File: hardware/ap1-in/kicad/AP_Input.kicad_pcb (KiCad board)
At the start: 2 copper layers, 72 x 56 mm, 66 parts, among them J1 QWIIC ENTRADA, J2 QWIIC SALIDA, J3 I2C, J4 I1-I3, J5 I4-I6, J6 I7-I8, J7 COM, U1 TCA9554PWR

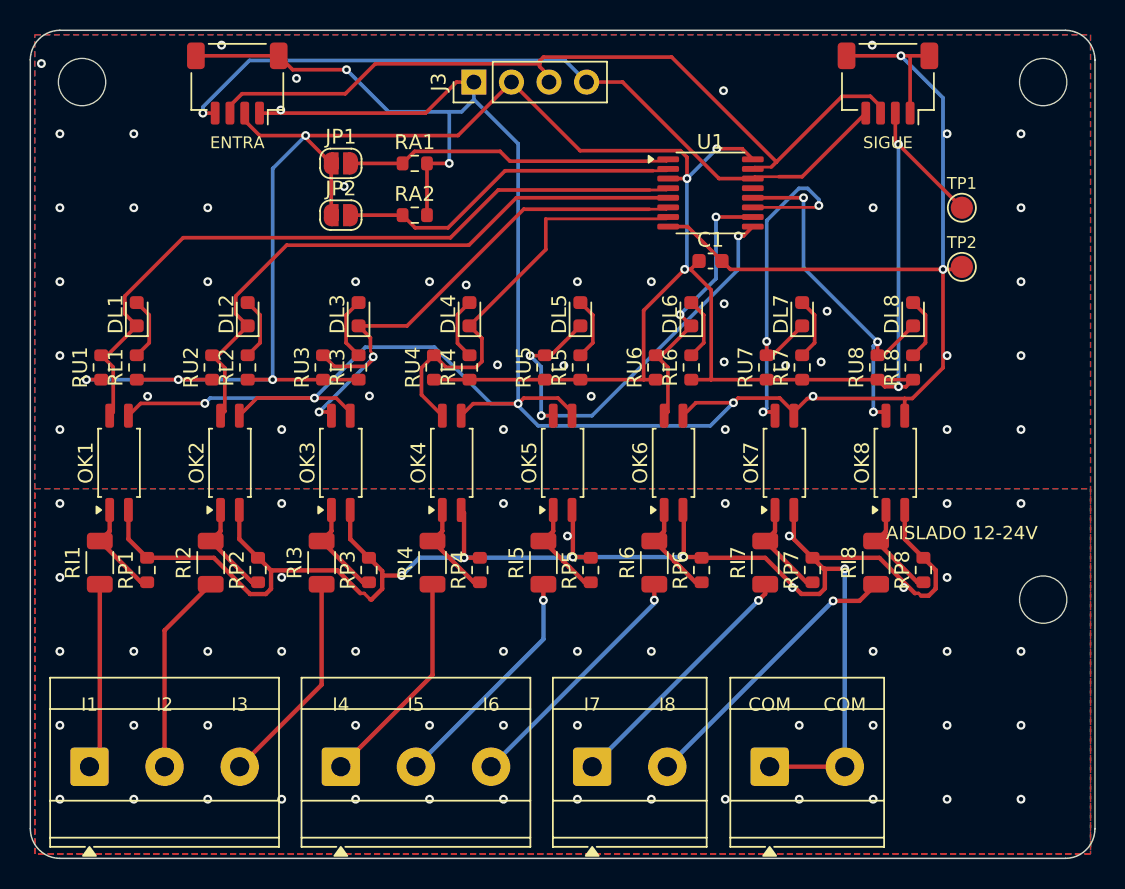
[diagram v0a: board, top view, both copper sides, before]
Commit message: AP CONNECT: sin borneras en todas las placas, placa nueva AP PRO AI4 y guía de fabricantes
- Borneras de tornillo reemplazadas por conectores con cable y código LCSC verificado:
  XT60 (C98732), JST VH 2/3/4 (C160315/6/7), JST XH 2/3/4 (C158012, C144394/5), Qwiic
  en BASE, IND, PIX, DMX, PLANTILLA, AP INPUT, AP OUTPUT y DIST 4; zonas de potencia rehechas
- XT60 de la DIST 4 con la polaridad marcada en la huella (pata 1 = -, pata 2 = +)
- TCA9554PWR ya con código (C477924)
- ap1-ai4: 4 entradas 0-10 V / 4-20 mA con ADS1115 (C37593), +24 V para sensores de lazo
- Programa 1.7: lectura AI4, umbrales con acciones, Home Assistant, tarjeta en la app
- FABRICANTES.md: JLCPCB, PCBWay, Seeed, NextPCB, México; impresión 3D y tornillería
- Pedido JLCPCB con 10 placas (AP-0.2 retirada); ERC/DRC/DFM 0 en todas

Co-Authored-By: Claude Opus 5.5 <noreply@anthropic.com>
Claude-Session: https://claude.ai/code/session_01WVk3oGwfQfGTmAT2PMp8oW
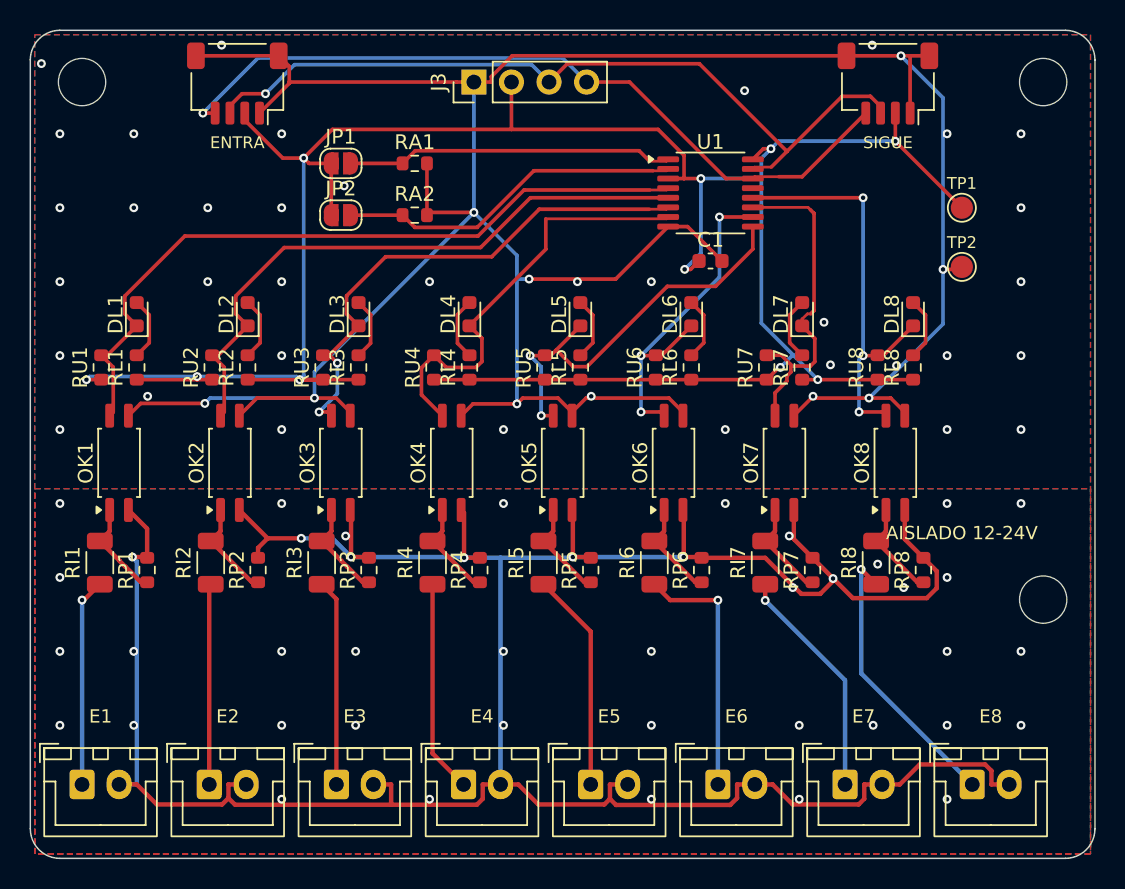
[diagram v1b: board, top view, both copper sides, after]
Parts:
- added J10: E7, Connector_JST:JST_XH_B2B-XH-A_1x02_P2.50mm_Vertical, F.Cu at (155.1, 151.0)
- added J11: E8, Connector_JST:JST_XH_B2B-XH-A_1x02_P2.50mm_Vertical, F.Cu at (163.7, 151.0)
- added J8: E5, Connector_JST:JST_XH_B2B-XH-A_1x02_P2.50mm_Vertical, F.Cu at (137.9, 151.0)
- added J9: E6, Connector_JST:JST_XH_B2B-XH-A_1x02_P2.50mm_Vertical, F.Cu at (146.5, 151.0)
- J4: value I1-I3 -> E1; footprint TerminalBlock_Phoenix:TerminalBlock_Phoenix_MKDS-3-3-5.08_1x03_P5.08mm_Horizontal -> Connector_JST:JST_XH_B2B-XH-A_1x02_P2.50mm_Vertical
- J5: value I4-I6 -> E2; footprint TerminalBlock_Phoenix:TerminalBlock_Phoenix_MKDS-3-3-5.08_1x03_P5.08mm_Horizontal -> Connector_JST:JST_XH_B2B-XH-A_1x02_P2.50mm_Vertical
- J6: value I7-I8 -> E3; footprint TerminalBlock_Phoenix:TerminalBlock_Phoenix_MKDS-3-2-5.08_1x02_P5.08mm_Horizontal -> Connector_JST:JST_XH_B2B-XH-A_1x02_P2.50mm_Vertical
- J7: value COM -> E4; footprint TerminalBlock_Phoenix:TerminalBlock_Phoenix_MKDS-3-2-5.08_1x02_P5.08mm_Horizontal -> Connector_JST:JST_XH_B2B-XH-A_1x02_P2.50mm_Vertical
- moved J7 20.7 mm to (129.3, 151.0)
- moved J6 17.3 mm to (120.7, 151.0)
- moved J5 8.98 mm to (112.1, 151.0)
- moved J4 1.30 mm to (103.5, 151.0)
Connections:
- J4 pad 2: /I2 -> /COM
- J5 pad 1: /I4 -> /I2
- J5 pad 2: /I5 -> /COM
- J6 pad 1: /I7 -> /I3
- J6 pad 2: /I8 -> /COM
- J7 pad 1: /COM -> /I4
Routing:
- net /COM: track 119.9 -> 192.2 mm, vias 54 -> 43
- net /GND: track 204.6 -> 197.0 mm, vias 52 -> 46
- net /IN7: track 27.8 -> 22.7 mm, vias 3 -> 0
- net /IN6: track 18.9 -> 23.5 mm, vias 2 -> 3
- net /3V3: track 174.0 -> 170.6 mm, vias 9 -> 10
- net /IN8: track 25.2 -> 28.2 mm
- net /IN5: track 30.4 -> 28.0 mm, vias 3 -> 2
- net /IN3: track 37.0 -> 35.3 mm
- net /I1: track 12.6 -> 14.1 mm, vias 0 -> 1
- net /I7: track 17.2 -> 15.8 mm
- net /I5: track 15.9 -> 14.9 mm, vias 1 -> 0
- net /I3: track 14.6 -> 14.0 mm
- net /SDA: track 54.8 -> 54.2 mm, vias 0 -> 1
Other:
- board text added: "E1"
- board text added: "E2"
- board text added: "E3"
- board text added: "E4"
- board text added: "E5"
- board text added: "E6"
- board text added: "E7"
- board text added: "E8"
- board text removed: "COM"
- board text removed: "I1"
- board text removed: "I2"
- board text removed: "I3"
- board text removed: "I4"
- board text removed: "I5"
- board text removed: "I6"
- board text removed: "I7"
- board text removed: "I8"
